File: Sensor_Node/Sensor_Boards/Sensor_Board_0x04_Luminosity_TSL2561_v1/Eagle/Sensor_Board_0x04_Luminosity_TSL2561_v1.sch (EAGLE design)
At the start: 15 parts, among them J1 M04_SMD_90, J2 M06_SMD_STRAIGHT, J4 ARDUINO_ISP, U2 ATMEGA328P_TQFP, Y1 8MHZ

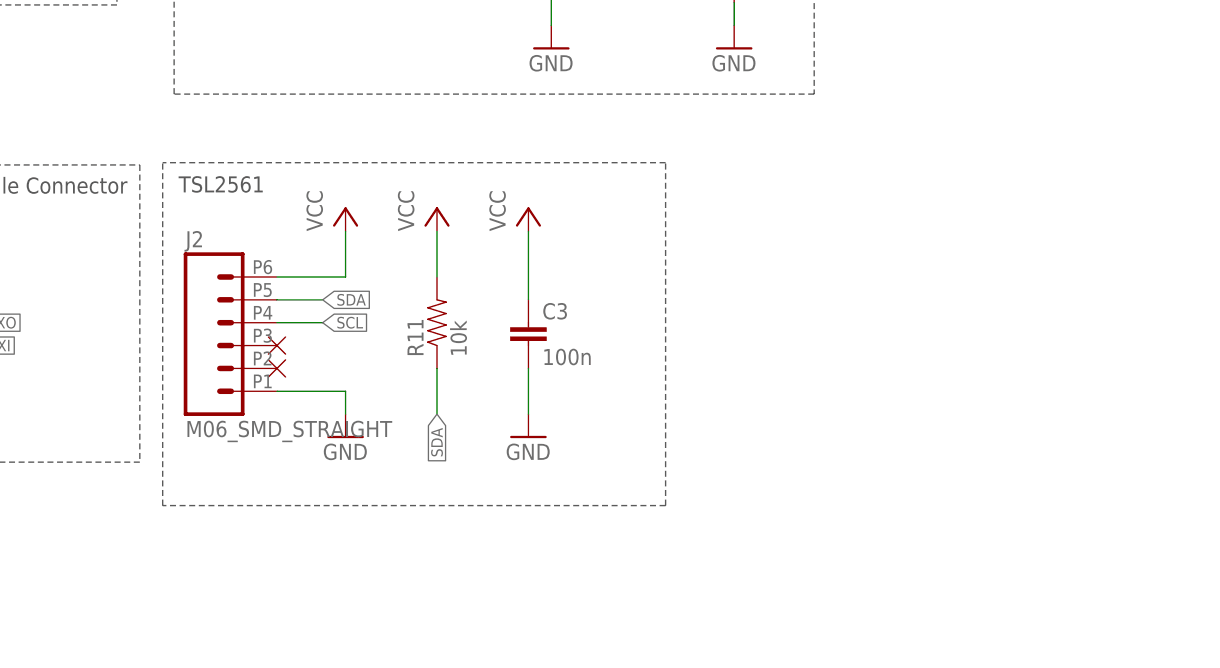
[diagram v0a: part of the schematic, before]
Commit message: Changes on SensModule TSL2561
- removed R11
- added pogohead programming connector
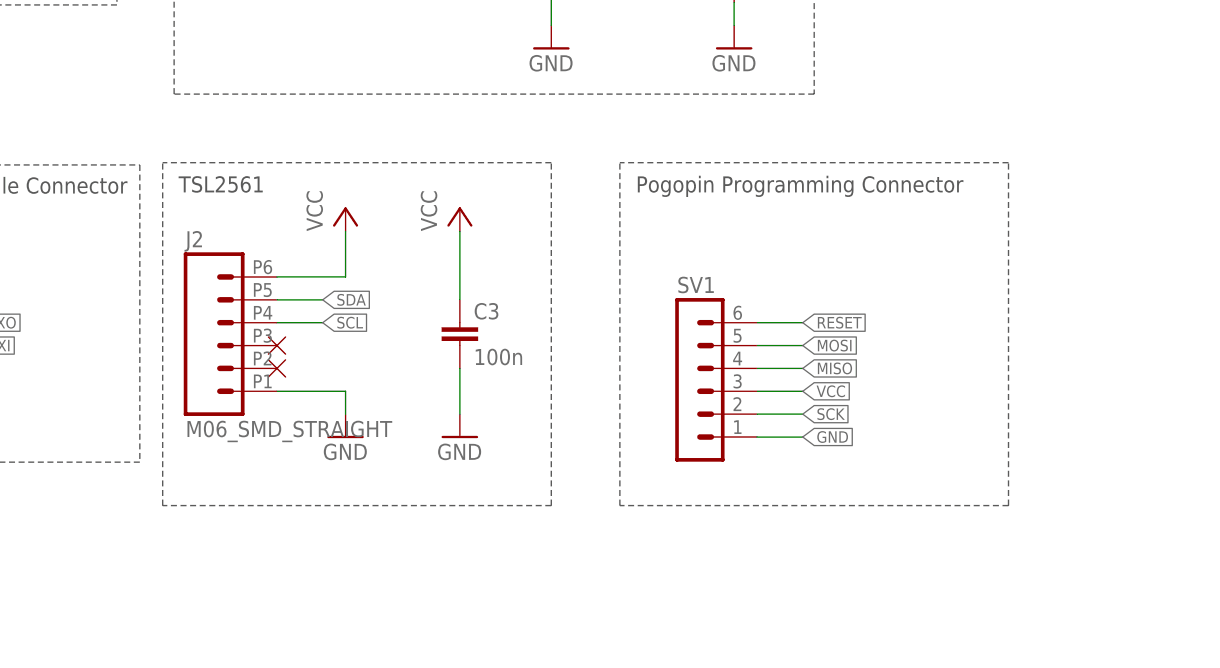
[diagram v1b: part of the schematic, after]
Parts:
- removed R11: 10k, SparkFun-Passives:RESISTOR0805-RES
- added SV1: (no value), con-lstb:MA06-1
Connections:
- net GND: now also SV1.1
- net MISO: now also SV1.4
- net MOSI: now also SV1.5
- net RESET: now also SV1.6
- net SCK: now also SV1.2
- net SDA: no longer R11.1
- net VCC: now also SV1.3; no longer R11.2
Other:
- note added: "Pogopin Programming Connector"
- moved on the sheet: C3
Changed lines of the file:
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@@
 <layers>
 <layer number="1" name="Top" color="4" fill="1" visible="no" active="no"/>
+<layer number="2" name="Route2" color="1" fill="3" visible="no" active="no"/>
+<layer number="3" name="Route3" color="4" fill="3" visible="no" active="no"/>
+<layer number="4" name="Route4" color="1" fill="4" visible="no" active="no"/>
+<layer number="5" name="Route5" color="4" fill="4" visible="no" active="no"/>
+<layer number="6" name="Route6" color="1" fill="8" visible="no" active="no"/>
+<layer number="7" name="Route7" color="4" fill="8" visible="no" active="no"/>
+<layer number="8" name="Route8" color="1" fill="2" visible="no" active="no"/>
+<layer number="9" name="Route9" color="4" fill="2" visible="no" active="no"/>
+<layer number="10" name="Route10" color="1" fill="7" visible="no" active="no"/>
+<layer number="11" name="Route11" color="4" fill="7" visible="no" active="no"/>
+<layer number="12" name="Route12" color="1" fill="5" visible="no" active="no"/>
+<layer number="13" name="Route13" color="4" fill="5" visible="no" active="no"/>
+<layer number="14" name="Route14" color="1" fill="6" visible="no" active="no"/>
+<layer number="15" name="Route15" color="4" fill="6" visible="no" active="no"/>
 <layer number="16" name="Bottom" color="1" fill="1" visible="no" active="no"/>
 <layer number="17" name="Pads" color="2" fill="1" visible="no" active="no"/>
@@
 <part name="GND2" library="SparkFun-Aesthetics" deviceset="GND" device=""/>
 <part name="GND10" library="supply1" deviceset="GND" device=""/>
-<part name="R11" library="SparkFun-Passives" deviceset="RESISTOR" device="0805-RES" value="10k"/>
 <part name="C3" library="eagle-ltspice" deviceset="C" device="" value="100n"/>
 <part name="GND11" library="SparkFun" deviceset="GND" device=""/>
@@
 <part name="P+5" library="supply1" deviceset="VCC" device=""/>
 <part name="P+16" library="supply1" deviceset="VCC" device=""/>
-<part name="P+17" library="supply1" deviceset="VCC" device=""/>
 <part name="P+20" library="supply1" deviceset="VCC" device=""/>
 <part name="S3" library="myownthings" deviceset="JS202011SCQN" device=""/>
@@
 <part name="U$20" library="myownthings" deviceset="N/C" device=""/>
 <part name="J1" library="myownthings" deviceset="M04_SMD_90" device=""/>
+<part name="SV1" library="con-lstb" deviceset="MA06-1" device=""/>
 </parts>
 <sheets>
@@
 <wire x1="48.26" y1="30.226" x2="7.62" y2="30.226" width="0.1524" layer="97" style="shortdash"/>
 <text x="8.89" y="60.071" size="1.778" layer="97">Communication Module Connector</text>
-<wire x1="106.68" y1="63.5" x2="50.8" y2="63.5" width="0.1524" layer="97" style="shortdash"/>
-<wire x1="106.68" y1="25.4" x2="50.8" y2="25.4" width="0.1524" layer="97" style="shortdash"/>
+<wire x1="93.98" y1="63.5" x2="50.8" y2="63.5" width="0.1524" layer="97" style="shortdash"/>
+<wire x1="93.98" y1="25.4" x2="50.8" y2="25.4" width="0.1524" layer="97" style="shortdash"/>
 <wire x1="50.8" y1="25.4" x2="50.8" y2="63.5" width="0.1524" layer="97" style="shortdash"/>
-<wire x1="106.68" y1="25.4" x2="106.68" y2="63.5" width="0.1524" layer="97" style="shortdash"/>
+<wire x1="93.98" y1="25.4" x2="93.98" y2="63.5" width="0.1524" layer="97" style="shortdash"/>
 <text x="52.578" y="60.198" size="1.778" layer="97">TSL2561</text>
 <text x="224.52133125" y="11.3923625" size="2.54" layer="94" font="vector">Sensor Board - TSL2561</text>
 <text x="277.84098125" y="1.169803125" size="2.54" layer="94" font="vector">1.0</text>
+<wire x1="144.78" y1="63.5" x2="101.6" y2="63.5" width="0.1524" layer="97" style="shortdash"/>
+<wire x1="144.78" y1="25.4" x2="101.6" y2="25.4" width="0.1524" layer="97" style="shortdash"/>
+<wire x1="101.6" y1="25.4" x2="101.6" y2="63.5" width="0.1524" layer="97" style="shortdash"/>
+<wire x1="144.78" y1="25.4" x2="144.78" y2="63.5" width="0.1524" layer="97" style="shortdash"/>
+<text x="103.378" y="60.198" size="1.778" layer="97">Pogopin Programming Connector</text>
 </plain>
 <instances>
@@
 <instance part="GND2" gate="1" x="25.4" y="35.56"/>
 <instance part="GND10" gate="1" x="71.12" y="33.02"/>
-<instance part="R11" gate="G$1" x="81.28" y="45.72" rot="R90"/>
-<instance part="C3" gate="G$1" x="91.44" y="45.72"/>
-<instance part="GND11" gate="1" x="91.44" y="33.02"/>
+<instance part="C3" gate="G$1" x="83.82" y="45.72"/>
+<instance part="GND11" gate="1" x="83.82" y="33.02"/>
 <instance part="P+1" gate="VCC" x="25.4" y="198.12"/>
 <instance part="P+2" gate="VCC" x="33.02" y="172.72"/>
@@
 <instance part="P+5" gate="VCC" x="25.4" y="53.34"/>
 <instance part="P+16" gate="VCC" x="71.12" y="58.42"/>
-<instance part="P+17" gate="VCC" x="81.28" y="58.42"/>
-<instance part="P+20" gate="VCC" x="91.44" y="58.42"/>
+<instance part="P+20" gate="VCC" x="83.82" y="58.42"/>
 <instance part="S3" gate="G$1" x="101.6" y="93.98"/>
 <instance part="U$1" gate="G$1" x="86.36" y="180.34"/>
@@
 <instance part="U$20" gate="G$1" x="63.5" y="40.64"/>
 <instance part="J1" gate="G$1" x="15.24" y="45.72" rot="MR180"/>
+<instance part="SV1" gate="1" x="109.22" y="40.64"/>
 </instances>
 <busses>
@@
 <pinref part="C3" gate="G$1" pin="2"/>
 <pinref part="GND11" gate="1" pin="GND"/>
-<wire x1="91.44" y1="35.56" x2="91.44" y2="40.64" width="0.1524" layer="91"/>
+<wire x1="83.82" y1="35.56" x2="83.82" y2="40.64" width="0.1524" layer="91"/>
 </segment>
 <segment>
@@
 <wire x1="96.52" y1="91.44" x2="93.98" y2="91.44" width="0.1524" layer="91"/>
 <wire x1="93.98" y1="91.44" x2="93.98" y2="78.74" width="0.1524" layer="91"/>
+</segment>
+<segment>
+<pinref part="SV1" gate="1" pin="1"/>
+<wire x1="116.84" y1="33.02" x2="121.92" y2="33.02" width="0.1524" layer="91"/>
+<label x="121.92" y="33.02" size="1.27" layer="95" xref="yes"/>
 </segment>
 </net>
@@
 </segment>
 <segment>
-<pinref part="R11" gate="G$1" pin="2"/>
-<pinref part="P+17" gate="VCC" pin="VCC"/>
-<wire x1="81.28" y1="50.8" x2="81.28" y2="55.88" width="0.1524" layer="91"/>
-</segment>
-<segment>
 <pinref part="P+16" gate="VCC" pin="VCC"/>
 <wire x1="71.12" y1="50.8" x2="71.12" y2="55.88" width="0.1524" layer="91"/>
@@
 <pinref part="C3" gate="G$1" pin="1"/>
 <pinref part="P+20" gate="VCC" pin="VCC"/>
-<wire x1="91.44" y1="48.26" x2="91.44" y2="55.88" width="0.1524" layer="91"/>
+<wire x1="83.82" y1="48.26" x2="83.82" y2="55.88" width="0.1524" layer="91"/>
+</segment>
+<segment>
+<pinref part="SV1" gate="1" pin="3"/>
+<wire x1="116.84" y1="38.1" x2="121.92" y2="38.1" width="0.1524" layer="91"/>
+<label x="121.92" y="38.1" size="1.27" layer="95" xref="yes"/>
 </segment>
 </net>
@@
 <pinref part="J4" gate="G$1" pin="RST"/>
 </segment>
+<segment>
+<pinref part="SV1" gate="1" pin="6"/>
+<wire x1="116.84" y1="45.72" x2="121.92" y2="45.72" width="0.1524" layer="91"/>
+<label x="121.92" y="45.72" size="1.27" layer="95" xref="yes"/>
+</segment>
 </net>
 <net name="SCK" class="0">
@@
 <pinref part="U2" gate="U$1" pin="PB5(SCK)"/>
 </segment>
+<segment>
+<pinref part="SV1" gate="1" pin="2"/>
+<wire x1="116.84" y1="35.56" x2="121.92" y2="35.56" width="0.1524" layer="91"/>
+<label x="121.92" y="35.56" size="1.27" layer="95" xref="yes"/>
+</segment>
 </net>
 <net name="MISO" class="0">
@@
 <pinref part="U2" gate="U$1" pin="PB4(MISO)"/>
 </segment>
+<segment>
+<pinref part="SV1" gate="1" pin="4"/>
+<wire x1="116.84" y1="40.64" x2="121.92" y2="40.64" width="0.1524" layer="91"/>
+<label x="121.92" y="40.64" size="1.27" layer="95" xref="yes"/>
+</segment>
 </net>
 <net name="MOSI" class="0">
@@
 <pinref part="U2" gate="U$1" pin="PB3(MOSI/OC2)"/>
 </segment>
+<segment>
+<pinref part="SV1" gate="1" pin="5"/>
+<wire x1="116.84" y1="43.18" x2="121.92" y2="43.18" width="0.1524" layer="91"/>
+<label x="121.92" y="43.18" size="1.27" layer="95" xref="yes"/>
+</segment>
 </net>
 <net name="MCU_TXO" class="0">
@@
 </segment>
 <segment>
-<pinref part="R11" gate="G$1" pin="1"/>
-<wire x1="81.28" y1="35.56" x2="81.28" y2="40.64" width="0.1524" layer="91"/>
-<label x="81.28" y="35.56" size="1.27" layer="95" rot="R270" xref="yes"/>
-</segment>
-<segment>

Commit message: Changes on SensModule TSL2561
- minor changes on schema
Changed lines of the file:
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@@
 <part name="J1" library="myownthings" deviceset="M04_SMD_90" device=""/>
 <part name="SV1" library="con-lstb" deviceset="MA06-1" device=""/>
+<part name="GND1" library="SparkFun" deviceset="GND" device=""/>
+<part name="P+6" library="supply1" deviceset="VCC" device=""/>
 </parts>
 <sheets>
@@
 <instance part="J1" gate="G$1" x="15.24" y="45.72" rot="MR180"/>
 <instance part="SV1" gate="1" x="109.22" y="40.64"/>
+<instance part="GND1" gate="1" x="134.62" y="27.94"/>
+<instance part="P+6" gate="VCC" x="134.62" y="53.34"/>
 </instances>
 <busses>
@@
 <segment>
 <pinref part="SV1" gate="1" pin="1"/>
-<wire x1="116.84" y1="33.02" x2="121.92" y2="33.02" width="0.1524" layer="91"/>
-<label x="121.92" y="33.02" size="1.27" layer="95" xref="yes"/>
+<wire x1="116.84" y1="33.02" x2="134.62" y2="33.02" width="0.1524" layer="91"/>
+<pinref part="GND1" gate="1" pin="GND"/>
+<wire x1="134.62" y1="33.02" x2="134.62" y2="30.48" width="0.1524" layer="91"/>
 </segment>
 </net>
@@
 </segment>
 <segment>
+<pinref part="P+6" gate="VCC" pin="VCC"/>
+<wire x1="134.62" y1="50.8" x2="134.62" y2="38.1" width="0.1524" layer="91"/>
 <pinref part="SV1" gate="1" pin="3"/>
-<wire x1="116.84" y1="38.1" x2="121.92" y2="38.1" width="0.1524" layer="91"/>
-<label x="121.92" y="38.1" size="1.27" layer="95" xref="yes"/>
+<wire x1="134.62" y1="38.1" x2="116.84" y2="38.1" width="0.1524" layer="91"/>
 </segment>
 </net>

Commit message: Changes on all boards
- added capacitor on reset-path
- changed order of pogopin programmer pins

Pulse-Board:
- Deleted input-jumper. Currently one interrupt-pin missing, so print is
not yet routed.
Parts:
- added C1: 100n, eagle-ltspice:C
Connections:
- new net N$4: C1.2, R5.1, S1.RIGHT, U2.PC6(/RESET)
- net MISO: now also SV1.6; no longer SV1.4
- net MOSI: now also SV1.2; no longer SV1.5
- net RESET: now also C1.1, SV1.4; no longer R5.1, S1.RIGHT, SV1.6, U2.PC6(/RESET)
- net SCK: now also SV1.5; no longer SV1.2
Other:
- moved on the sheet: C10, C9, R5, S1, U2, Y1

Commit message: Changed some SensorBoards
SHT31
- new routing

PULSE
- pogopin programmer now over FTDI
- interrupt to comboard now comes from atmega

TSL2561
- pogopin programmer now over FTDI

PROTOYPING
- changed title of schematic
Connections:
- new net FTDI_RXI: SV1.4, U2.PD0(RXD)
- new net FTDI_TXO: SV1.5, U2.PD1(TXD)
- net GND: now also SV1.2
- net MCU_RXI: now also U2.PD7(AIN1); no longer U2.PD0(RXD)
- net MCU_TXO: now also U2.PD6(AIN0); no longer U2.PD1(TXD)
- net MISO: no longer SV1.6
- net MOSI: no longer SV1.2
- net RESET: now also SV1.6; no longer SV1.4
- net SCK: no longer SV1.5
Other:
- note added: "FTDI Pogopin Connector"
- note removed: "Pogopin Programming Connector"
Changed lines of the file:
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@@
 <part name="U$7" library="myownthings" deviceset="N/C" device=""/>
 <part name="U$8" library="myownthings" deviceset="N/C" device=""/>
-<part name="U$9" library="myownthings" deviceset="N/C" device=""/>
-<part name="U$10" library="myownthings" deviceset="N/C" device=""/>
 <part name="U$11" library="myownthings" deviceset="N/C" device=""/>
 <part name="U$12" library="myownthings" deviceset="N/C" device=""/>
@@
 <wire x1="101.6" y1="25.4" x2="101.6" y2="63.5" width="0.1524" layer="97" style="shortdash"/>
 <wire x1="144.78" y1="25.4" x2="144.78" y2="63.5" width="0.1524" layer="97" style="shortdash"/>
-<text x="103.378" y="60.198" size="1.778" layer="97">Pogopin Programming Connector</text>
+<text x="103.378" y="60.198" size="1.778" layer="97">FTDI Pogopin Connector</text>
 </plain>
 <instances>
@@
 <instance part="U$7" gate="G$1" x="109.22" y="152.4"/>
 <instance part="U$8" gate="G$1" x="109.22" y="149.86"/>
-<instance part="U$9" gate="G$1" x="109.22" y="147.32"/>
-<instance part="U$10" gate="G$1" x="109.22" y="144.78"/>
 <instance part="U$11" gate="G$1" x="109.22" y="142.24"/>
 <instance part="U$12" gate="G$1" x="109.22" y="139.7"/>
@@
 <pinref part="GND1" gate="1" pin="GND"/>
 <wire x1="134.62" y1="33.02" x2="134.62" y2="30.48" width="0.1524" layer="91"/>
+<pinref part="SV1" gate="1" pin="2"/>
+<wire x1="116.84" y1="35.56" x2="134.62" y2="35.56" width="0.1524" layer="91"/>
+<wire x1="134.62" y1="35.56" x2="134.62" y2="33.02" width="0.1524" layer="91"/>
+<junction x="134.62" y="33.02"/>
 </segment>
 </net>
@@
 </segment>
 <segment>
-<pinref part="SV1" gate="1" pin="4"/>
-<wire x1="116.84" y1="40.64" x2="121.92" y2="40.64" width="0.1524" layer="91"/>
-<label x="121.92" y="40.64" size="1.27" layer="95" xref="yes"/>
+<pinref part="SV1" gate="1" pin="6"/>
+<wire x1="116.84" y1="45.72" x2="121.92" y2="45.72" width="0.1524" layer="91"/>
+<label x="121.92" y="45.72" size="1.27" layer="95" xref="yes"/>
 </segment>
 </net>
@@
 <pinref part="U2" gate="U$1" pin="PB5(SCK)"/>
 </segment>
-<segment>
-<pinref part="SV1" gate="1" pin="5"/>
-<wire x1="116.84" y1="43.18" x2="121.92" y2="43.18" width="0.1524" layer="91"/>
-<label x="121.92" y="43.18" size="1.27" layer="95" xref="yes"/>
-</segment>
 </net>
 <net name="MISO" class="0">
@@
 <pinref part="U2" gate="U$1" pin="PB4(MISO)"/>
 </segment>
-<segment>
-<pinref part="SV1" gate="1" pin="6"/>
-<wire x1="116.84" y1="45.72" x2="121.92" y2="45.72" width="0.1524" layer="91"/>
-<label x="121.92" y="45.72" size="1.27" layer="95" xref="yes"/>
-</segment>
 </net>
 <net name="MOSI" class="0">
@@
 <pinref part="U2" gate="U$1" pin="PB3(MOSI/OC2)"/>
 </segment>
-<segment>
-<pinref part="SV1" gate="1" pin="2"/>
-<wire x1="116.84" y1="35.56" x2="121.92" y2="35.56" width="0.1524" layer="91"/>
-<label x="121.92" y="35.56" size="1.27" layer="95" xref="yes"/>
-</segment>
 </net>
 <net name="MCU_TXO" class="0">
-<segment>
-<wire x1="109.22" y1="160.02" x2="111.76" y2="160.02" width="0.1524" layer="91"/>
-<label x="111.76" y="160.02" size="1.27" layer="95" xref="yes"/>
-<pinref part="U2" gate="U$1" pin="PD1(TXD)"/>
-</segment>
 <segment>
 <wire x1="20.32" y1="45.72" x2="25.4" y2="45.72" width="0.1524" layer="91"/>
@@
 <pinref part="J1" gate="G$1" pin="2"/>
 </segment>
+<segment>
+<pinref part="U2" gate="U$1" pin="PD6(AIN0)"/>
+<wire x1="109.22" y1="147.32" x2="111.76" y2="147.32" width="0.1524" layer="91"/>
+<label x="111.76" y="147.32" size="1.27" layer="95" xref="yes"/>
+</segment>
 </net>
 <net name="SCL" class="0">
@@
 <net name="MCU_RXI" class="0">
 <segment>
-<wire x1="109.22" y1="162.56" x2="111.76" y2="162.56" width="0.1524" layer="91"/>
-<label x="111.76" y="162.56" size="1.27" layer="95" xref="yes"/>
-<pinref part="U2" gate="U$1" pin="PD0(RXD)"/>
-</segment>
-<segment>
 <wire x1="20.32" y1="43.18" x2="25.4" y2="43.18" width="0.1524" layer="91"/>
 <label x="25.4" y="43.18" size="1.27" layer="95" xref="yes"/>
 <pinref part="J1" gate="G$1" pin="3"/>
+</segment>
+<segment>
+<pinref part="U2" gate="U$1" pin="PD7(AIN1)"/>
+<wire x1="109.22" y1="144.78" x2="111.76" y2="144.78" width="0.1524" layer="91"/>
+<label x="111.76" y="144.78" size="1.27" layer="95" xref="yes"/>
 </segment>
 </net>
@@
 </segment>
 </net>
+<net name="FTDI_RXI" class="0">
+<segment>
+<wire x1="109.22" y1="162.56" x2="111.76" y2="162.56" width="0.1524" layer="91"/>
+<label x="111.76" y="162.56" size="1.27" layer="95" xref="yes"/>
+<pinref part="U2" gate="U$1" pin="PD0(RXD)"/>
+</segment>
+<segment>
+<pinref part="SV1" gate="1" pin="4"/>
+<wire x1="116.84" y1="40.64" x2="121.92" y2="40.64" width="0.1524" layer="91"/>
+<label x="121.92" y="40.64" size="1.27" layer="95" xref="yes"/>
+</segment>
+</net>
+<net name="FTDI_TXO" class="0">
+<segment>
+<wire x1="109.22" y1="160.02" x2="111.76" y2="160.02" width="0.1524" layer="91"/>
+<label x="111.76" y="160.02" size="1.27" layer="95" xref="yes"/>
+<pinref part="U2" gate="U$1" pin="PD1(TXD)"/>
+</segment>
+<segment>
+<pinref part="SV1" gate="1" pin="5"/>
+<wire x1="116.84" y1="43.18" x2="121.92" y2="43.18" width="0.1524" layer="91"/>
+<label x="121.92" y="43.18" size="1.27" layer="95" xref="yes"/>
+</segment>
+</net>

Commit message: Updated schematic description
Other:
- note added: "Sensor Board - TSL2561 (0x04)"
- note removed: "Sensor Board - TSL2561"
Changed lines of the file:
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@@
 <wire x1="93.98" y1="25.4" x2="93.98" y2="63.5" width="0.1524" layer="97" style="shortdash"/>
 <text x="52.578" y="60.198" size="1.778" layer="97">TSL2561</text>
-<text x="224.52133125" y="11.3923625" size="2.54" layer="94" font="vector">Sensor Board - TSL2561</text>
+<text x="224.52133125" y="11.3923625" size="2.54" layer="94" font="vector">Sensor Board - TSL2561 (0x04)</text>
 <text x="277.84098125" y="1.169803125" size="2.54" layer="94" font="vector">1.0</text>
 <wire x1="144.78" y1="63.5" x2="101.6" y2="63.5" width="0.1524" layer="97" style="shortdash"/>
